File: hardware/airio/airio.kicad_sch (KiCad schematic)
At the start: 0 parts

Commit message: Draw airio v0 schematic
XIAO nRF52840 carrier with BMP581 baro and LSM6DSV16X IMU on I2C, differential
piezo, user button, LiPo connector and SWD test pads, following the pin map in
docs/airio-parts-and-pinmap.md. Adds a project symbol library for the XIAO and
both sensors, and a PDF plot.

Co-Authored-By: Claude Opus 5.5 (1M context) <noreply@anthropic.com>
Claude-Session: https://claude.ai/code/session_019xhAfw8yP418EQ5rHrNZbT
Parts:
- added BZ1: PKLCS1212E4001, Buzzer_Beeper:Buzzer_Murata_PKLCS1212E, symbol Device:Buzzer
- added C1, C2, C3, C4: 100n, Capacitor_SMD:C_0603_1608Metric, symbol Device:C
- added J1: LiPo 1S, Connector_JST:JST_PH_S2B-PH-SM4-TB_1x02-1MP_P2.00mm_Horizontal, symbol Connector_Generic:Conn_01x02
- added R1, R2: 4.7k, Resistor_SMD:R_0603_1608Metric, symbol Device:R
- added SW1: TS-1187A-B-A-B, Button_Switch_SMD:SW_Push_1P1T_XKB_TS-1187A, symbol Switch:SW_Push
- added TP1: SWDIO, TestPoint:TestPoint_Pad_D1.0mm, symbol Connector:TestPoint
- added TP2: SWCLK, TestPoint:TestPoint_Pad_D1.0mm, symbol Connector:TestPoint
- added TP3: XIAO_RST, TestPoint:TestPoint_Pad_D1.0mm, symbol Connector:TestPoint
- added TP4: VBAT, TestPoint:TestPoint_Pad_D1.0mm, symbol Connector:TestPoint
- added TP5: +3V3, TestPoint:TestPoint_Pad_D1.0mm, symbol Connector:TestPoint
- added TP6: GND, TestPoint:TestPoint_Pad_D1.0mm, symbol Connector:TestPoint
- added U1: XIAO nRF52840, symbol airio:XIAO_nRF52840
- added U2: BMP581, symbol airio:BMP581
- added U3: LSM6DSV16X, Package_LGA:LGA-14_3x2.5mm_P0.5mm_LayoutBorder3x4y, symbol airio:LSM6DSV16X
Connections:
- new net +3V3: C1.1, C2.1, C3.1, C4.1, R1.1, R2.1, TP5.1, U1.12 (3V3), U2.1 (VDDIO), U2.10 (VDD), U2.5 (SDO), U2.6 (CSB), U3.12 (CS), U3.5 (VDDIO), U3.8 (VDD)
- new net BARO_INT: U1.2 (D1), U2.7 (INT)
- new net BTN: SW1.1, U1.7 (D6)
- new net BUZZ_A: BZ1.1 (+), U1.3 (D2)
- new net BUZZ_B: BZ1.2 (-), U1.4 (D3)
- new net GND: C1.2, C2.2, C3.2, C4.2, J1.2 (Pin_2), SW1.2, TP6.1, U1.13 (GND), U1.16 (BAT-), U1.20 (GND), U2.3 (VSS), U2.8 (VSS), U2.9 (VSS), U3.1 (SDO/SA0), U3.2 (SDx/Qvar1), U3.3 (SCx/Qvar2), U3.6 (GND), U3.7 (GND)
- new net I2C_SCL: R2.2, U1.6 (D5_SCL), U2.2 (SCK), U3.13 (SCL)
- new net I2C_SDA: R1.2, U1.5 (D4_SDA), U2.4 (SDI), U3.14 (SDA)
- new net IMU_INT1: U1.1 (D0), U3.4 (INT1)
- new net SWCLK: TP2.1, U1.18 (SWCLK)
- new net SWDIO: TP1.1, U1.17 (SWDIO)
- new net VBAT: J1.1 (Pin_1), TP4.1, U1.15 (BAT+)
- new net XIAO_RST: TP3.1, U1.19 (~{RST})
- no-connect marks 0 -> 10
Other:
- note added: "BZ1 Piezo beeper"
- note added: "Board notes: keep U2 away from the XIAO antenna end and regulator, under a foam cover with a vent. Put U3 near the board centre, away from screws. The XIAO antenna end overhangs the carrier or sits over a copper keepout."
- note added: "C1 at VDDIO (pin 1), C2 at VDD (pin 10), each close to its pin."
- note added: "C3 at VDDIO (pin 5), C4 at VDD (pin 8). Qvar pins 2-3 to GND."
- note added: "Charged by the XIAO through its BAT+ / BAT- underside pads."
- note added: "Debug pads"
- note added: "Driven differentially by PWM0 ch0/ch1, about 6.6 Vpp."
- note added: "I2C address 0x47: SDO and CSB tied to 3V3."
- note added: "I2C address 0x6A: SDO/SA0 to GND, CS to 3V3."
- note added: "I2C pull-ups"
- note added: "INT2 and aux SPI (pins 10-11) unused."
- note added: "J1 1S LiPo, about 150 mAh"
- note added: "Onboard: 3.3 V LDO (3V3 pin), BQ25101 LiPo charger, USB-C, UF2 bootloader. Internal, no carrier connection: P0.31 VBAT_SENSE, P0.14 VBAT_SENSE_EN, P0.17 CHG_STAT, P0.13 CHG_ISET. Spares: D7-D10 (SPI/UART), NFC1/NFC2."
- note added: "Pin 1 = +. Check the cell lead polarity before plugging in."
- note added: "SW1 User / power button"
- note added: "SWD for a J-Link or Pico debug probe, wired to the XIAO underside pads."
- note added: "To 3V3, bus runs at 400 kHz."
- note added: "To GND, internal pull-up. Wakes from System OFF."
- note added: "U1 Seeed XIAO nRF52840 (non-Sense)"
- note added: "U2 Barometer (BMP581)"
- note added: "U3 IMU (LSM6DSV16X)"

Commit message: airio schematic: beeper is on PWM1, I2C is i2c1
Co-Authored-By: Claude Opus 5.5 (1M context) <noreply@anthropic.com>
Claude-Session: https://claude.ai/code/session_019xhAfw8yP418EQ5rHrNZbT
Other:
- note added: "Driven differentially by PWM1 ch0/ch1, about 6.6 Vpp."
- note added: "To 3V3, i2c1 at 400 kHz."
- note removed: "Driven differentially by PWM0 ch0/ch1, about 6.6 Vpp."
- note removed: "To 3V3, bus runs at 400 kHz."
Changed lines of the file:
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@@
     (effects (font (size 1.524 1.524) bold) (justify left bottom))
   )
-  (text "To 3V3, bus runs at 400 kHz." (at 129.54 40.64 0)
+  (text "To 3V3, i2c1 at 400 kHz." (at 129.54 40.64 0)
     (effects (font (size 1.27 1.27)) (justify left bottom))
   )
@@
     (effects (font (size 1.524 1.524) bold) (justify left bottom))
   )
-  (text "Driven differentially by PWM0 ch0/ch1, about 6.6 Vpp." (at 20.32 139.7 0)
-    (effects (font (size 1.27 1.27)) (justify left bottom))
-  )
+  (text "Driven differentially by PWM1 ch0/ch1, about 6.6 Vpp." (at 20.32 139.7 0)
+    (effects (font (size 1.27 1.27)) (justify left bottom))
+  )

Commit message: airio: KiCad 10 format, XIAO and BMP581 footprints, ERC
- Upgrade schematic, symbols and footprints to the KiCad 10 format.
- Add Seeed's XIAO-nRF52840-SMD footprint and a Bosch LGA-10 2x2 mm
  footprint for the BMP581/BMP580 in airio.pretty, plus fp-lib-table.
- Renumber the XIAO symbol's underside pins (SWD 15-18, BAT 19-20) to
  match Seeed's footprint.
- Swap the out-of-stock 100 nF cap C1591 for C66501.
- ERC in KiCad 10.0.7: 0 errors, 2 intended address-strap warnings.
- README: footprint notes, ERC result, priced parts list (CAD, LCSC stock).

Co-Authored-By: Claude Opus 5.5 (1M context) <noreply@anthropic.com>
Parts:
- C1, C2, C3, C4: LCSC C1591 -> C66501
- U1: footprint (none) -> airio:XIAO-nRF52840-SMD
- U2: footprint (none) -> airio:Bosch_LGA-10_2x2mm_P0.5mm
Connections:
- net GND: now also U1.18 (GND); no longer U1.16 (BAT-)
- net SWCLK: now also U1.16 (SWCLK); no longer U1.18 (SWCLK)
- net SWDIO: now also U1.15 (SWDIO); no longer U1.17 (SWDIO)
- net VBAT: now also U1.19 (BAT+); no longer U1.15 (BAT+)
- net XIAO_RST: now also U1.17 (~{RST}); no longer U1.19 (~{RST})

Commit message: airio: lay out the v0 PCB
- Add airio.kicad_pcb: 42 x 24 mm, two layers, 1.0 mm. XIAO on the right
  with USB-C at the top edge and its antenna end over a copper-free rule
  area; piezo and JST along the top, sensors lower middle, button bottom
  left; SWD/power test pads on the bottom.
- Ground poured and stitched on both layers; every net routed.
- airio.kicad_dru: allow the LSM6DSV16X LGA-14 pad gaps, 0.3 mm copper to
  edge, 0.15 mm minimum track. Board rules in airio.kicad_pro to match.
- DRC with schematic parity: 0 errors, 0 unconnected; only footprint
  silkscreen warnings remain.
- Schematic: test pads out of the BOM, stale footprint notes updated.
- README: PCB section and top render.

Co-Authored-By: Claude Opus 5.5 (1M context) <noreply@anthropic.com>
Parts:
- TP1, TP2, TP3, TP4, TP5, TP6: now left out of the parts list
- U1: Note Castellated module. Footprint with underside pads still to 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 -> Castellated module, soldered flat. Seeed SMD footprint.
- U2: Note Out of stock at LCSC: hand place. Footprint still to be mad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 -> Out of stock at LCSC: hand place, or fit the BMP580.
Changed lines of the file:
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@@
 		(body_style 1)
 		(exclude_from_sim no)
-		(in_bom yes)
+		(in_bom no)
 		(on_board yes)
 		(in_pos_files yes)
@@
 			)
 		)
-		(property "Note" "Castellated module. Footprint with underside pads still to be made."
+		(property "Note" "Castellated module, soldered flat. Seeed SMD footprint."
 			(at 101.6 91.44 0)
 			(hide yes)
@@
 			)
 		)
-		(property "Note" "Out of stock at LCSC: hand place. Footprint still to be made."
+		(property "Note" "Out of stock at LCSC: hand place, or fit the BMP580."
 			(at 203.2 66.04 0)
 			(hide yes)
@@
 		(body_style 1)
 		(exclude_from_sim no)
-		(in_bom yes)
+		(in_bom no)
 		(on_board yes)
 		(in_pos_files yes)
@@
 		(body_style 1)
 		(exclude_from_sim no)
-		(in_bom yes)
+		(in_bom no)
 		(on_board yes)
 		(in_pos_files yes)
@@
 		(body_style 1)
 		(exclude_from_sim no)
-		(in_bom yes)
+		(in_bom no)
 		(on_board yes)
 		(in_pos_files yes)
@@
 		(body_style 1)
 		(exclude_from_sim no)
-		(in_bom yes)
+		(in_bom no)
 		(on_board yes)
 		(in_pos_files yes)
@@
 		(body_style 1)
 		(exclude_from_sim no)
-		(in_bom yes)
+		(in_bom no)
 		(on_board yes)
 		(in_pos_files yes)

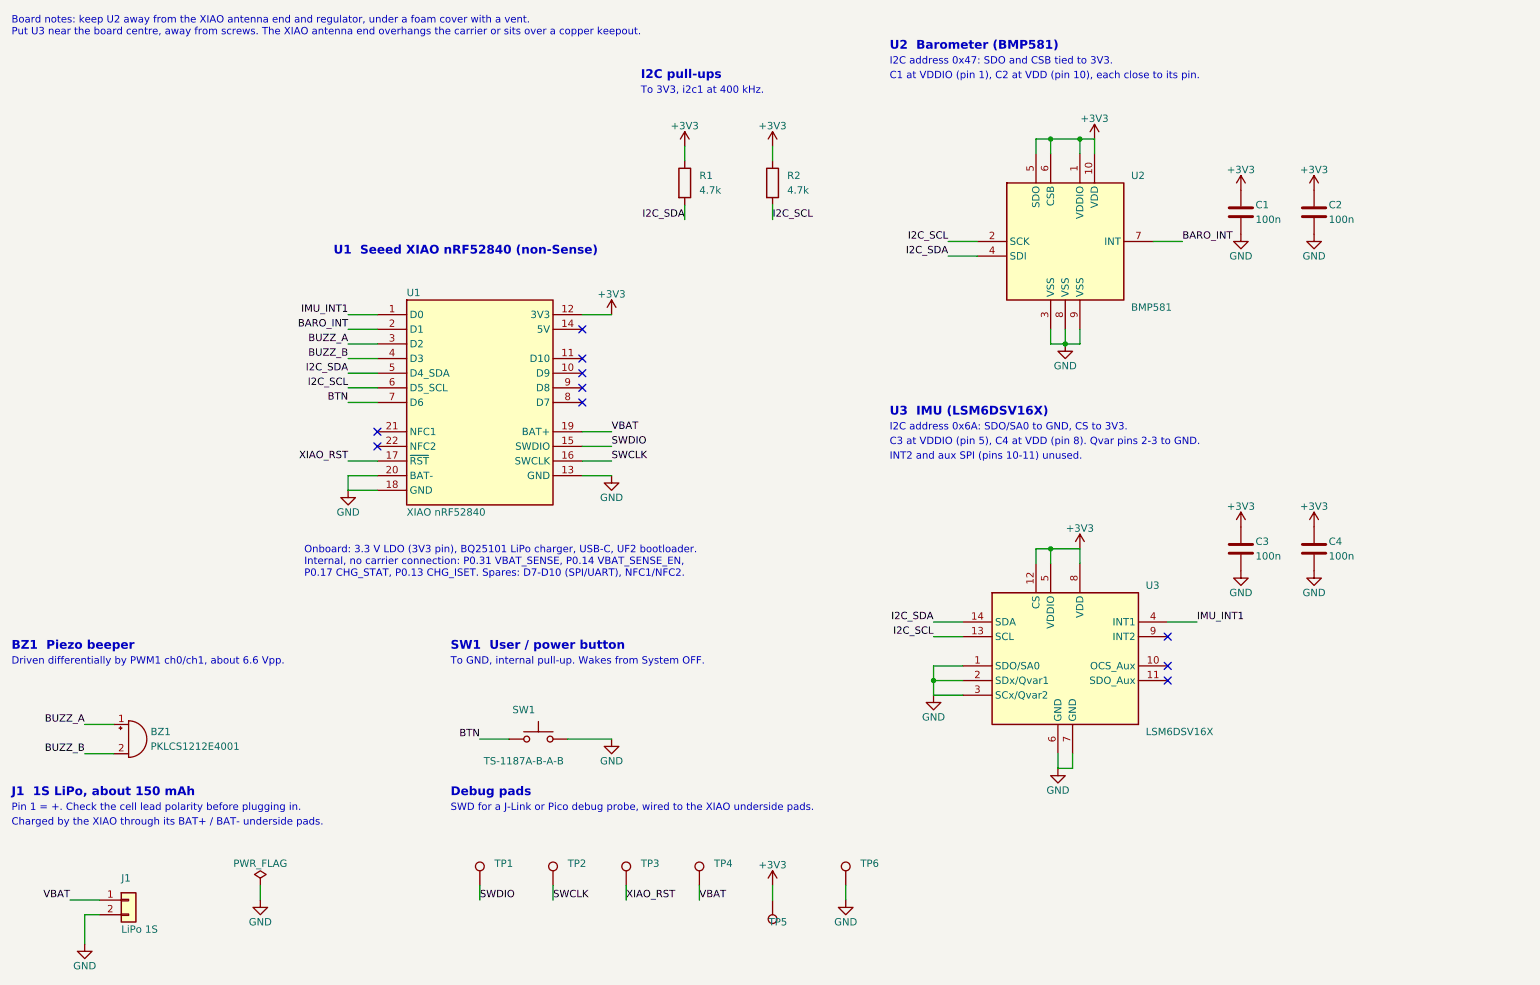
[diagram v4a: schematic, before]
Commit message: airio: add GPS, screen and spare I2C JST-PH ports
- Schematic: J2 GPS UART (GND, 3V3, GPS TX to D7, GPS RX from NFC1),
  J3 screen (GND, 3V3, VBAT, SCK D8, MOSI D10, CS D9, DISP NFC2, pin 8 NC),
  J4 spare I2C (GND, 3V3, SDA, SCL). B4B/B8B-PH-K vertical THT, pin 1 GND.
- Board widened from 42 to 54 mm; ports in a 12 mm strip on the left,
  placement only. Antenna keepout moved with the XIAO.
- ERC 0 errors; DRC with schematic parity has no footprint errors.
- Pin map and parts tables updated; BMP581 back in stock.

Co-Authored-By: Claude Opus 5.5 (1M context) <noreply@anthropic.com>
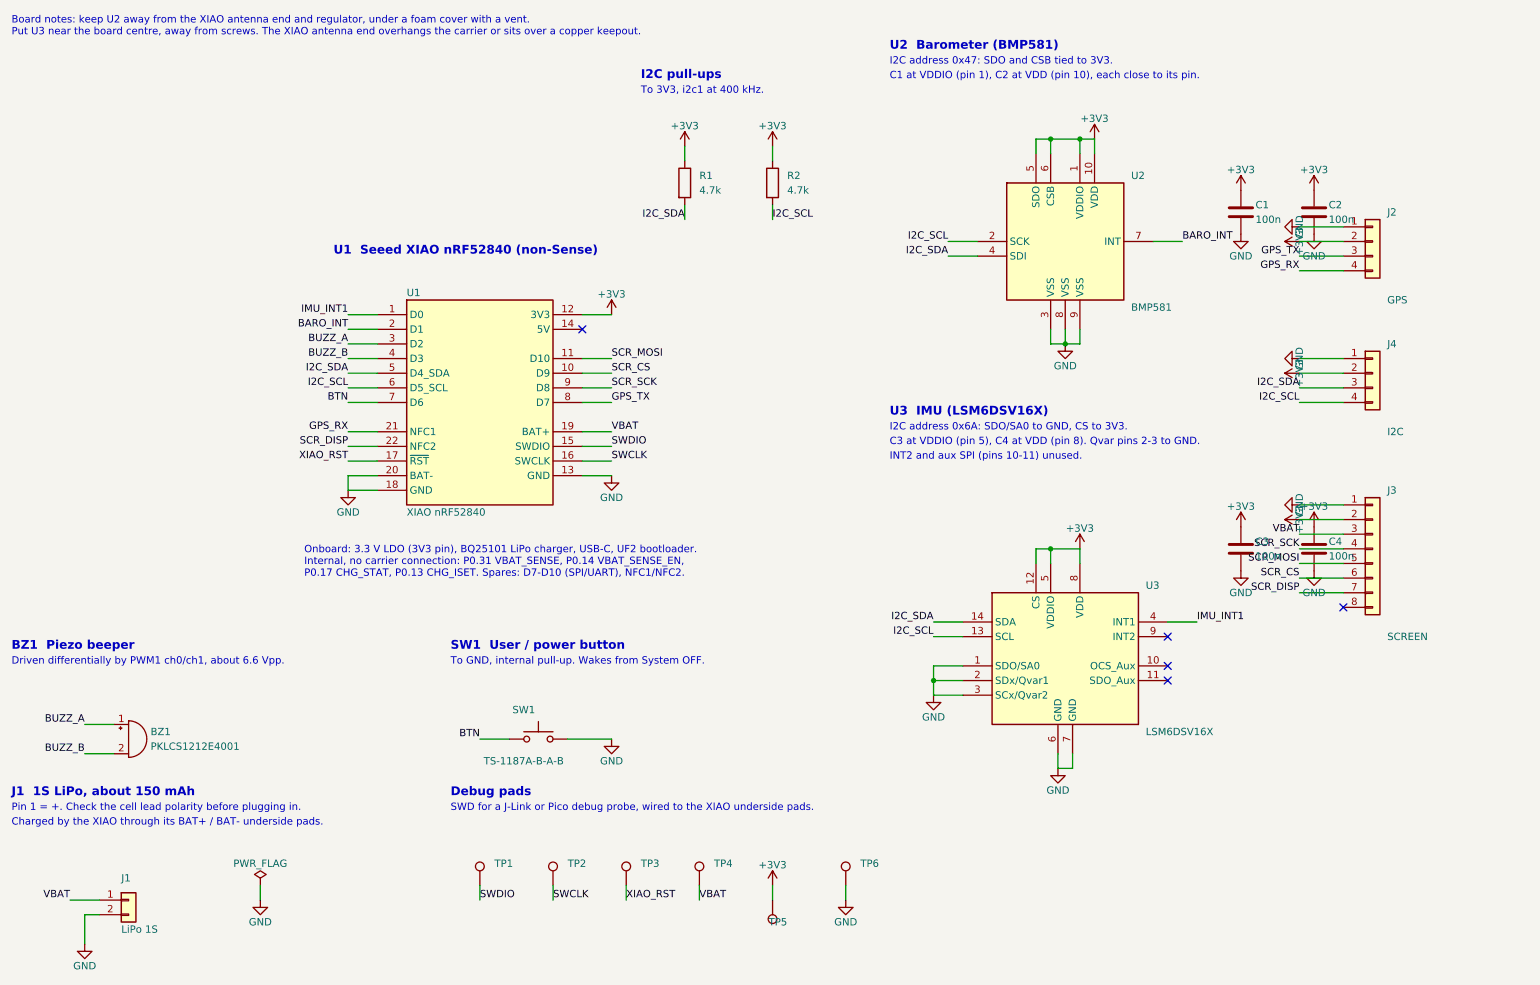
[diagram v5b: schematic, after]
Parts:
- added J2: GPS, Connector_JST:JST_PH_B4B-PH-K_1x04_P2.00mm_Vertical, symbol Connector_Generic:Conn_01x04
- added J3: SCREEN, Connector_JST:JST_PH_B8B-PH-K_1x08_P2.00mm_Vertical, symbol Connector_Generic:Conn_01x08
- added J4: I2C, Connector_JST:JST_PH_B4B-PH-K_1x04_P2.00mm_Vertical, symbol Connector_Generic:Conn_01x04
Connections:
- net +3V3: now also J2.2 (Pin_2), J3.2 (Pin_2), J4.2 (Pin_2)
- net GND: now also J2.1 (Pin_1), J3.1 (Pin_1), J4.1 (Pin_1)
- net I2C_SCL: now also J4.4 (Pin_4)
- net I2C_SDA: now also J4.3 (Pin_3)
- net VBAT: now also J3.3 (Pin_3)
- net SCR_CS: now reaches U1.10 (D9)
- net SCR_CS: now also J3.6 (Pin_6)
- net SCR_MOSI: now reaches U1.11 (D10)
- net SCR_MOSI: now also J3.5 (Pin_5)
- net GPS_RX: now reaches U1.21 (NFC1)
- net GPS_RX: now also J2.4 (Pin_4)
- net SCR_DISP: now reaches U1.22 (NFC2)
- net SCR_DISP: now also J3.7 (Pin_7)
- net GPS_TX: now reaches U1.8 (D7)
- net GPS_TX: now also J2.3 (Pin_3)
- net SCR_SCK: now reaches U1.9 (D8)
- net SCR_SCK: now also J3.4 (Pin_4)
- no-connect marks 10 -> 5

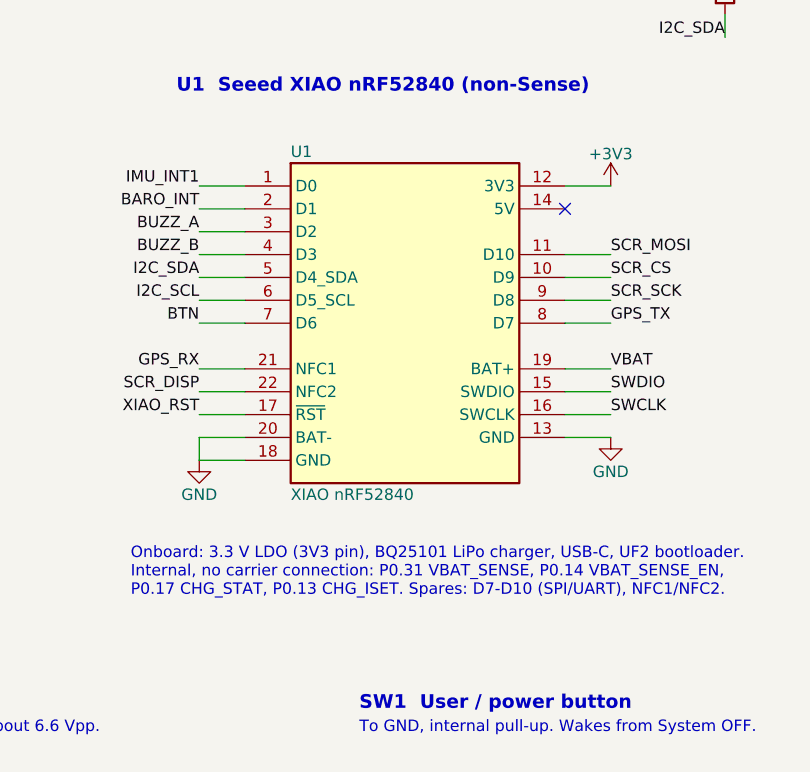
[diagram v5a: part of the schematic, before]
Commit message: airio: switch U1 to the XIAO nRF52840 Plus
The NFC pads carrying GPS_RX and SCR_DISP sat inside the antenna keepout,
so they could not be routed. The XIAO Plus has the same chip and outline
plus D11-D19 on half-pitch castellations away from the antenna.

- New symbol XIAO_nRF52840_Plus: GPS_RX on D12 (P0.19), SCR_DISP on D11
  (P0.15); SWD/RST/GND/battery pads renumbered 24-29 to Seeed's order.
- Footprint XIAO-nRF52840-Plus-SMD from Seeed's library, rotated so the
  main pads land where the standard XIAO's did; swapped in place on the
  board.
- ERC 0 errors; DRC with schematic parity has no footprint errors.
- Pin map and parts tables updated (Plus is not on LCSC).

Co-Authored-By: Claude Opus 5.5 (1M context) <noreply@anthropic.com>
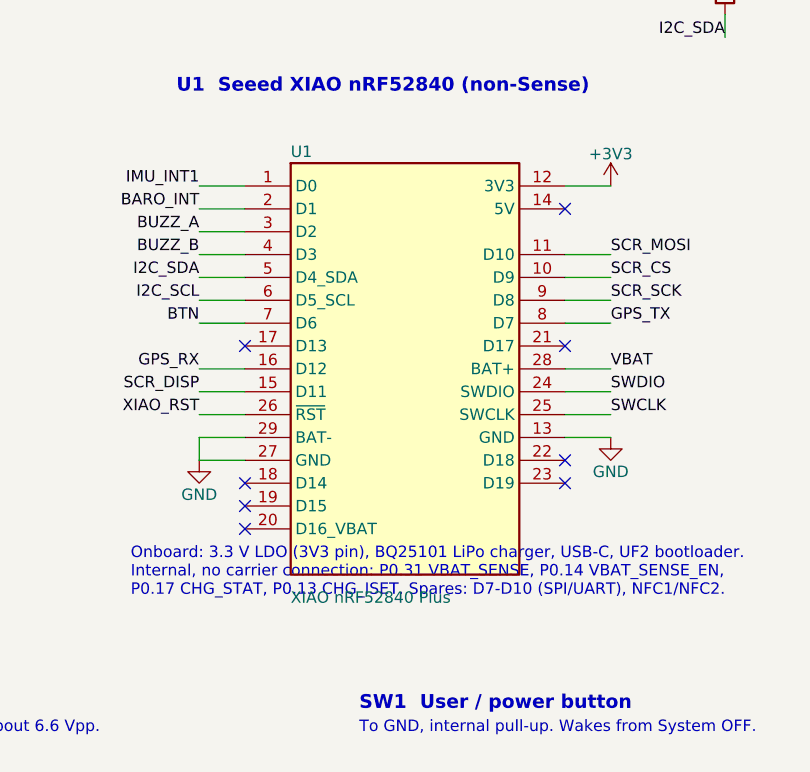
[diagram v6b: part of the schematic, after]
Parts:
- U1: value XIAO nRF52840 -> XIAO nRF52840 Plus; footprint airio:XIAO-nRF52840-SMD -> airio:XIAO-nRF52840-Plus-SMD; symbol airio:XIAO_nRF52840 -> airio:XIAO_nRF52840_Plus; LCSC C17209540 -> (none); MPN Seeed 102010448 -> Seeed 102010672; Note Castellated module, soldered flat. Seeed SMD footprint. -> Castellated module, soldered flat. Not on LCSC: buy from Se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
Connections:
- net GND: now also U1.27 (GND), U1.29 (BAT-); no longer U1.18 (GND), U1.20 (BAT-)
- net GPS_RX: now also U1.16 (D12); no longer U1.21 (NFC1)
- net SCR_DISP: now also U1.15 (D11); no longer U1.22 (NFC2)
- net SWCLK: now also U1.25 (SWCLK); no longer U1.16 (SWCLK)
- net SWDIO: now also U1.24 (SWDIO); no longer U1.15 (SWDIO)
- net VBAT: now also U1.28 (BAT+); no longer U1.19 (BAT+)
- net XIAO_RST: now also U1.26 (~{RST}); no longer U1.17 (~{RST})
- no-connect marks 5 -> 12
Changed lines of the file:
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@@
+	)
+	(no_connect
+		(at 83.82 116.84)
+	)
+	(no_connect
+		(at 119.38 111.76)
+	)
+	(no_connect
+		(at 83.82 96.52)
 	)
 	(no_connect
@@
 	)
 	(no_connect
+		(at 119.38 109.22)
+	)
+	(no_connect
 		(at 220.98 139.7)
 	)
@@
 	)
 	(no_connect
+		(at 119.38 96.52)
+	)
+	(no_connect
 		(at 220.98 134.62)
 	)
 	(no_connect
 		(at 119.38 81.28)
+	)
+	(no_connect
+		(at 83.82 114.3)
+	)
+	(no_connect
+		(at 83.82 111.76)
 	)
 	(wire
@@
 	)
 	(symbol
-		(lib_id "airio:XIAO_nRF52840")
+		(lib_id "airio:XIAO_nRF52840_Plus")
 		(at 101.6 91.44 0)
 		(unit 1)
@@
 			)
 		)
-		(property "Value" "XIAO nRF52840"
-			(at 88.9 113.03 0)
+		(property "Value" "XIAO nRF52840 Plus"
+			(at 88.9 124.46 0)
 			(show_name no)
 			(do_not_autoplace no)
@@
 			)
 		)
-		(property "Footprint" "airio:XIAO-nRF52840-SMD"
+		(property "Footprint" "airio:XIAO-nRF52840-Plus-SMD"
 			(at 101.6 91.44 0)
 			(hide yes)
@@
 			)
 		)
-		(property "LCSC" "C17209540"
+		(property "MPN" "Seeed 102010672"
 			(at 101.6 91.44 0)
 			(hide yes)
@@
 			)
 		)
-		(property "MPN" "Seeed 102010448"
+		(property "Note" "Castellated module, soldered flat. Not on LCSC: buy from Seeed and hand solder."
 			(at 101.6 91.44 0)
 			(hide yes)
@@
 			)
 		)
-		(property "Note" "Castellated module, soldered flat. Seeed SMD footprint."
-			(at 101.6 91.44 0)
-			(hide yes)
-			(show_name no)
-			(do_not_autoplace no)
-			(effects
-				(font
-					(size 1.27 1.27)
-				)
-			)
-		)
 		(pin "1"
 		)
@@
 		(pin "7"
 		)
+		(pin "8"
+		)
+		(pin "9"
+		)
+		(pin "10"
+		)
+		(pin "11"
+		)
+		(pin "12"
+		)
+		(pin "13"
+		)
+		(pin "14"
+		)
+		(pin "15"
+		)
+		(pin "16"
+		)
+		(pin "17"
+		)
+		(pin "18"
+		)
+		(pin "19"
+		)
+		(pin "20"
+		)
 		(pin "21"
 		)
 		(pin "22"
 		)
-		(pin "19"
-		)
-		(pin "16"
-		)
-		(pin "20"
-		)
-		(pin "12"
-		)
-		(pin "14"
-		)
-		(pin "11"
-		)
-		(pin "10"
-		)
-		(pin "9"
-		)
-		(pin "8"
-		)
-		(pin "15"
-		)
-		(pin "17"
-		)
-		(pin "18"
-		)
-		(pin "13"
+		(pin "23"
+		)
+		(pin "24"
+		)
+		(pin "25"
+		)
+		(pin "26"
+		)
+		(pin "27"
+		)
+		(pin "28"
+		)
+		(pin "29"
 		)
 		(instances
